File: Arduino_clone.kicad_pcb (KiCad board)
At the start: 2 copper layers, 0 parts

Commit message: Layout design rules edited
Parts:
- added BT1: Battery 3V, Connector_PinHeader_2.54mm:PinHeader_1x02_P2.54mm_Vertical, F.Cu at (151.2, 97.4)
- added C1: 22pF, Capacitor_SMD:C_0805_2012Metric_Pad1.18x1.45mm_HandSolder, F.Cu at (156.0, 96.5)
- added C2: 22pF, Capacitor_SMD:C_0805_2012Metric_Pad1.18x1.45mm_HandSolder, F.Cu at (156.0, 99.6)
- added C3: 10uF, Capacitor_SMD:C_0805_2012Metric_Pad1.18x1.45mm_HandSolder, F.Cu at (150.3, 103.7)
- added D1: LED, LED_SMD:LED_0805_2012Metric_Pad1.15x1.40mm_HandSolder, F.Cu at (150.3, 106.8)
- added J1: Serial, Connector_PinSocket_2.54mm:PinSocket_1x04_P2.54mm_Vertical, F.Cu at (138.4, 64.3)
- added J2: Digital pins, Connector_PinSocket_2.54mm:PinSocket_1x09_P2.54mm_Vertical, F.Cu at (129.2, 64.3)
- added J3: I2C, Connector_PinSocket_2.54mm:PinSocket_1x04_P2.54mm_Vertical, F.Cu at (133.8, 64.3)
- added J4: ICSP, Connector_PinSocket_2.54mm:PinSocket_2x03_P2.54mm_Vertical, F.Cu at (145.6, 64.3)
- added R1: 10k, Resistor_SMD:R_0805_2012Metric_Pad1.20x1.40mm_HandSolder, F.Cu at (155.1, 106.7)
- added R2: 330, Resistor_SMD:R_0805_2012Metric_Pad1.20x1.40mm_HandSolder, F.Cu at (155.1, 103.7)
- added U1: 24LC1025, Package_SO:SOIJ-8_5.3x5.3mm_P1.27mm, F.Cu at (143.6, 93.7)
- added U2: 24LC1025, Package_SO:SOIJ-8_5.3x5.3mm_P1.27mm, F.Cu at (132.2, 105.1)
- added U3: DS1337S+, Package_SO:SO-8_5.3x6.2mm_P1.27mm, F.Cu at (142.7, 105.5)
- added U4: ATMEGA328P-AU, digikey-footprints:TQFP-32_7x7mm, F.Cu at (132.6, 95.9)
- added Y1: 32 MHz, Crystal:Crystal_SMD_MicroCrystal_CC7V-T1A-2Pin_3.2x1.5mm_HandSoldering, F.Cu at (141.7, 98.9)
- added Y2: 16 MHz, Crystal:Crystal_SMD_5032-2Pin_5.0x3.2mm_HandSoldering, F.Cu at (154.0, 92.6)
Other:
- net class Power added: clearance 0.2, trace_width 0.3, via_dia 1, via_drill 0.6

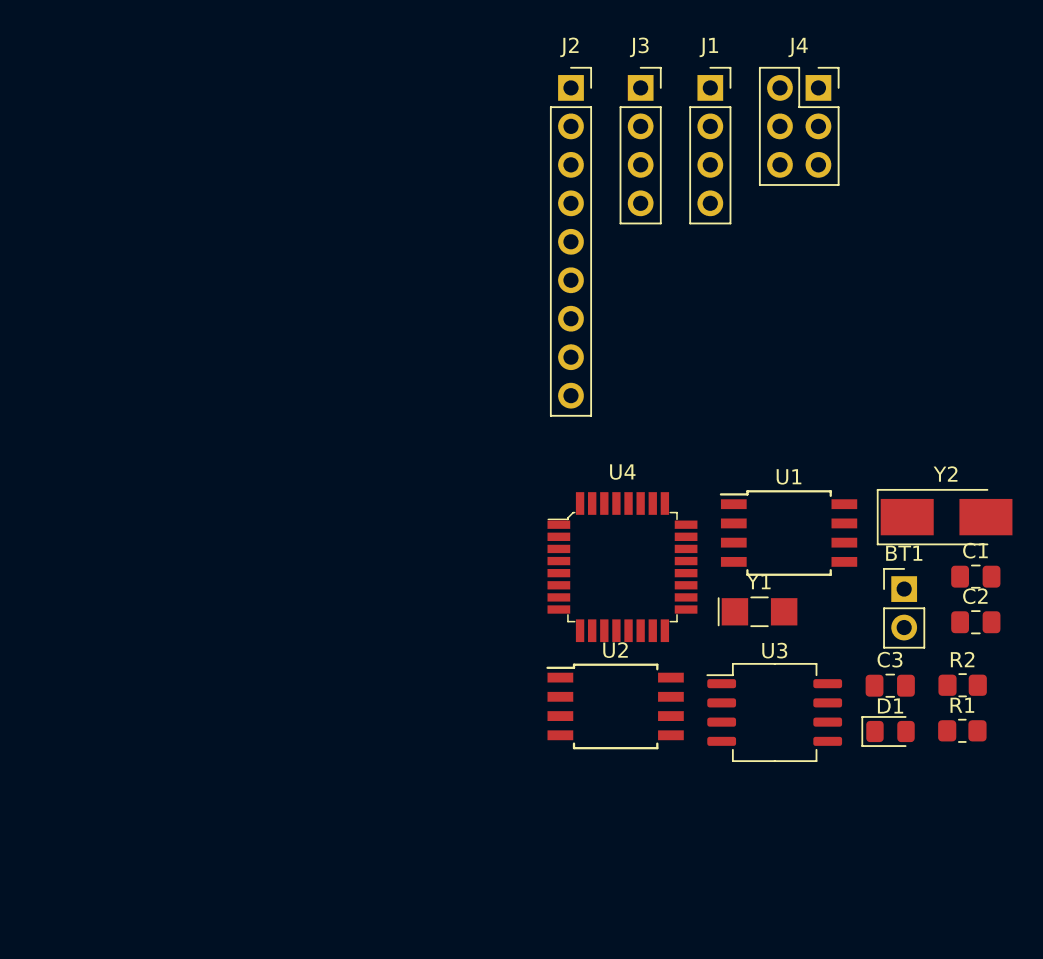
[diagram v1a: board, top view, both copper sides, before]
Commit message: Initial component placement done
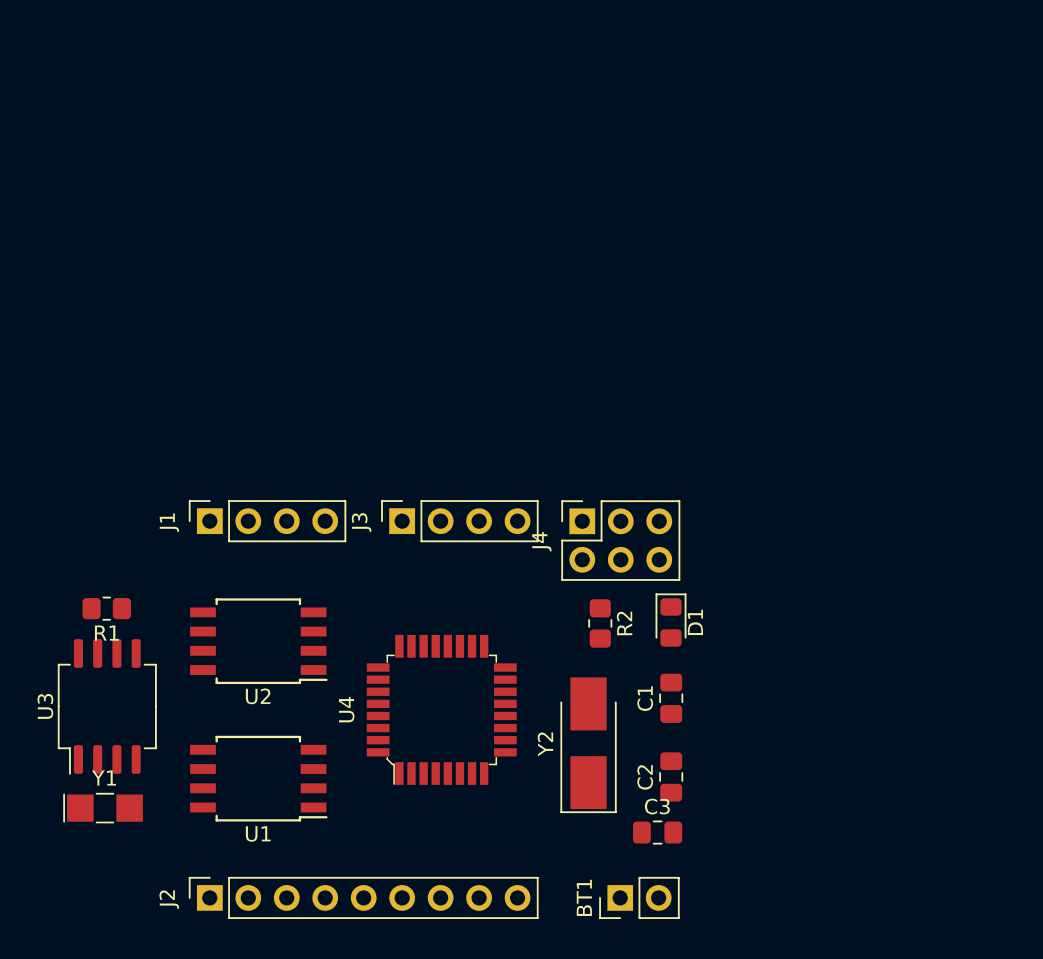
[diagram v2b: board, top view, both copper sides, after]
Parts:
- BT1: value Battery 3V -> 3V
- moved J2 58.6 mm to (105.4, 117.8), turned to 90 degrees
- moved R1 57.1 mm to (98.6, 98.7), turned to 180 degrees
- moved Y1 45.1 mm to (98.5, 111.8)
- moved U3 44.1 mm to (98.6, 105.1), turned to 90 degrees
- moved J1 43.7 mm to (105.4, 92.9), turned to 90 degrees
- moved U1 38.6 mm to (108.6, 109.9), turned to 180 degrees
- moved J3 32.7 mm to (118.1, 92.9), turned to 90 degrees
- moved J4 32.6 mm to (130.0, 92.9), turned to 90 degrees
- moved Y2 28.0 mm to (130.4, 107.5), turned to 90 degrees
- moved BT1 27.7 mm to (132.5, 117.8), turned to 90 degrees
- moved R2 24.3 mm to (131.2, 99.6), turned to 270 degrees
- moved U2 24.0 mm to (108.6, 100.8), turned to 180 degrees
- moved C2 22.6 mm to (135.9, 109.8), turned to 90 degrees
- moved C1 21.7 mm to (135.9, 104.6), turned to 90 degrees
- moved C3 18.2 mm to (135.0, 113.4)
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
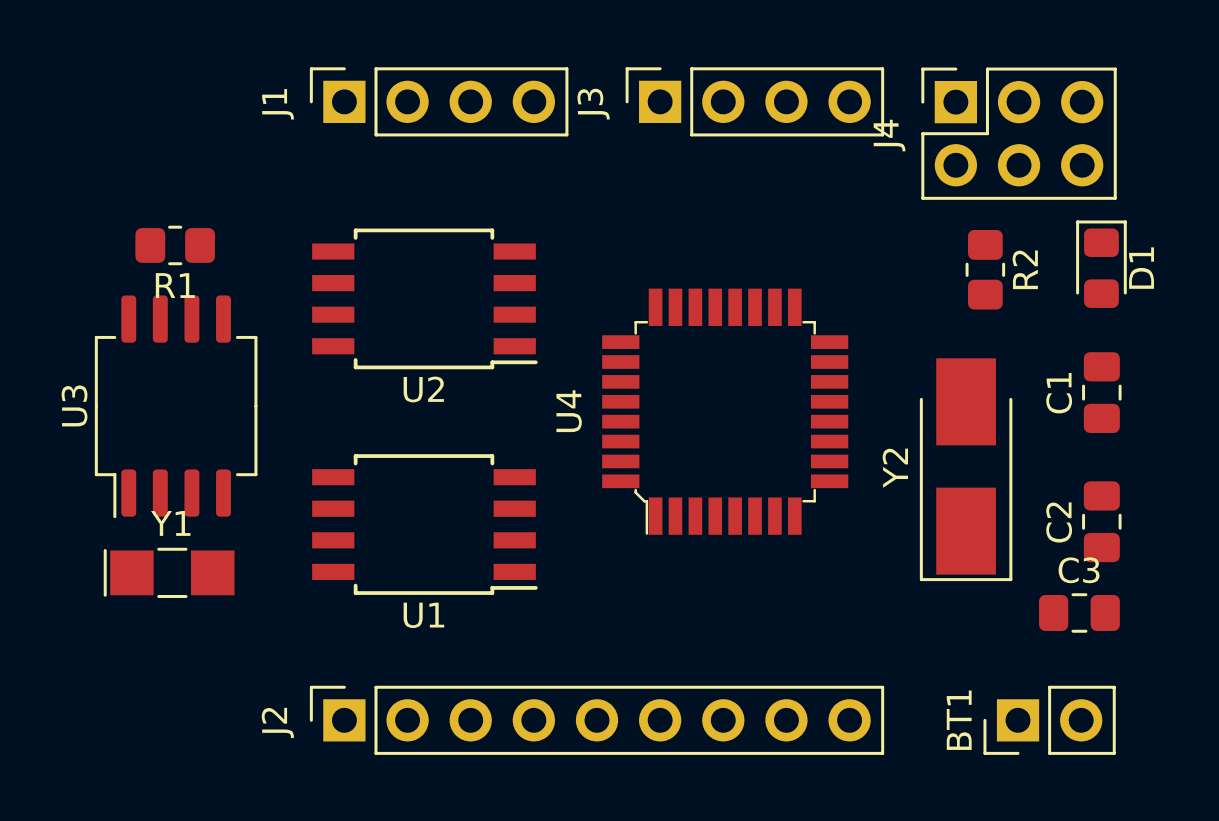
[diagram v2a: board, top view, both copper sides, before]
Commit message: Board outline drawn
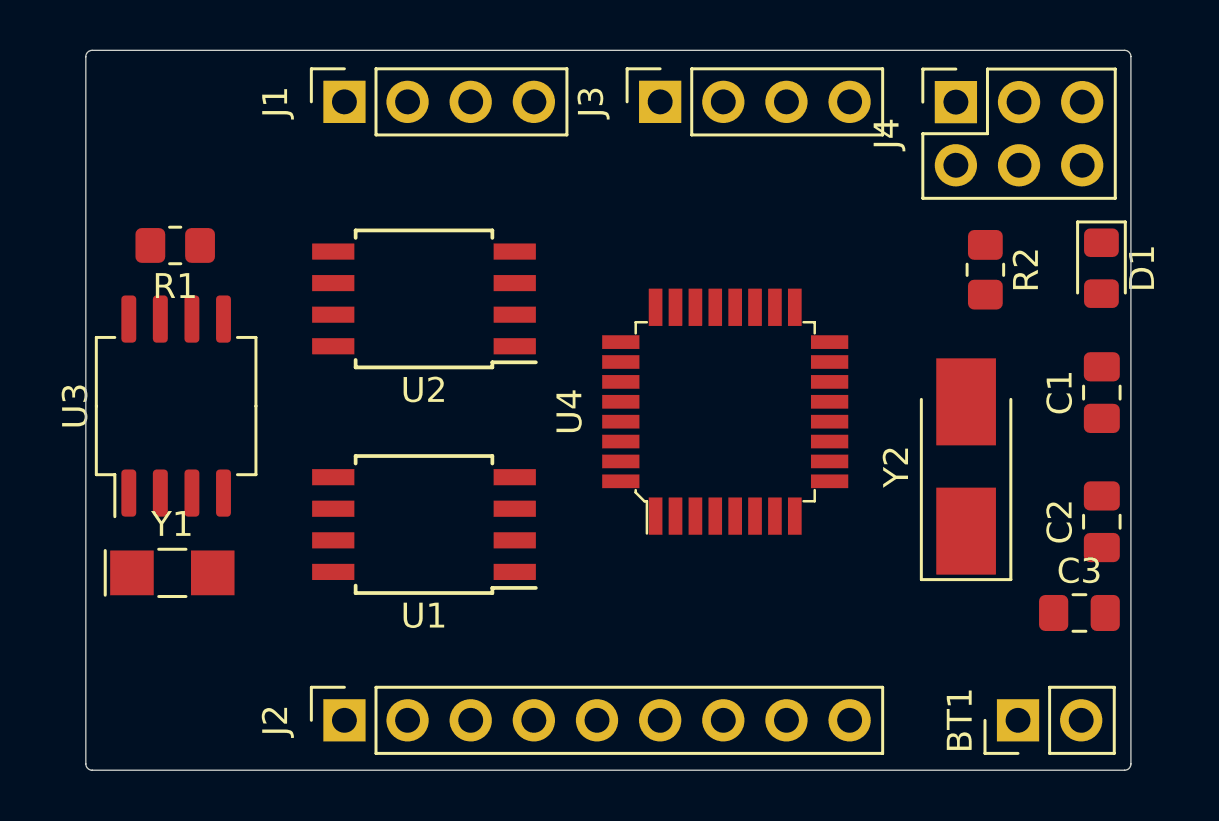
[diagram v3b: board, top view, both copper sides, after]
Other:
- board outline added: 42 x 29 mm
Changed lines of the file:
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@@
   (general
     (thickness 1.6)
-    (drawings 0)
+    (drawings 8)
     (tracks 0)
     (zones 0)
@@
     )
   )
+  (gr_line (start 95.25 90.805) (end 136.779 90.805) (layer Edge.Cuts) (width 0.05))
+  (gr_line (start 94.996 119.507) (end 94.996 91.059) (layer Edge.Cuts) (width 0.05))
+  (gr_line (start 95.25 119.761) (end 136.779 119.761) (layer Edge.Cuts) (width 0.05))
+  (gr_line (start 137.033 91.059) (end 137.033 119.507) (layer Edge.Cuts) (width 0.05))
+  (gr_arc (start 136.779 119.507) (end 136.779 119.761) (angle -90) (layer Edge.Cuts) (width 0.05))
+  (gr_arc (start 95.25 119.507) (end 94.996 119.507) (angle -90) (layer Edge.Cuts) (width 0.05))
+  (gr_arc (start 95.25 91.059) (end 95.25 90.805) (angle -90) (layer Edge.Cuts) (width 0.05))
+  (gr_arc (start 136.779 91.059) (end 137.033 91.059) (angle -90) (layer Edge.Cuts) (width 0.05))
 )

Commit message: Mounting holes added
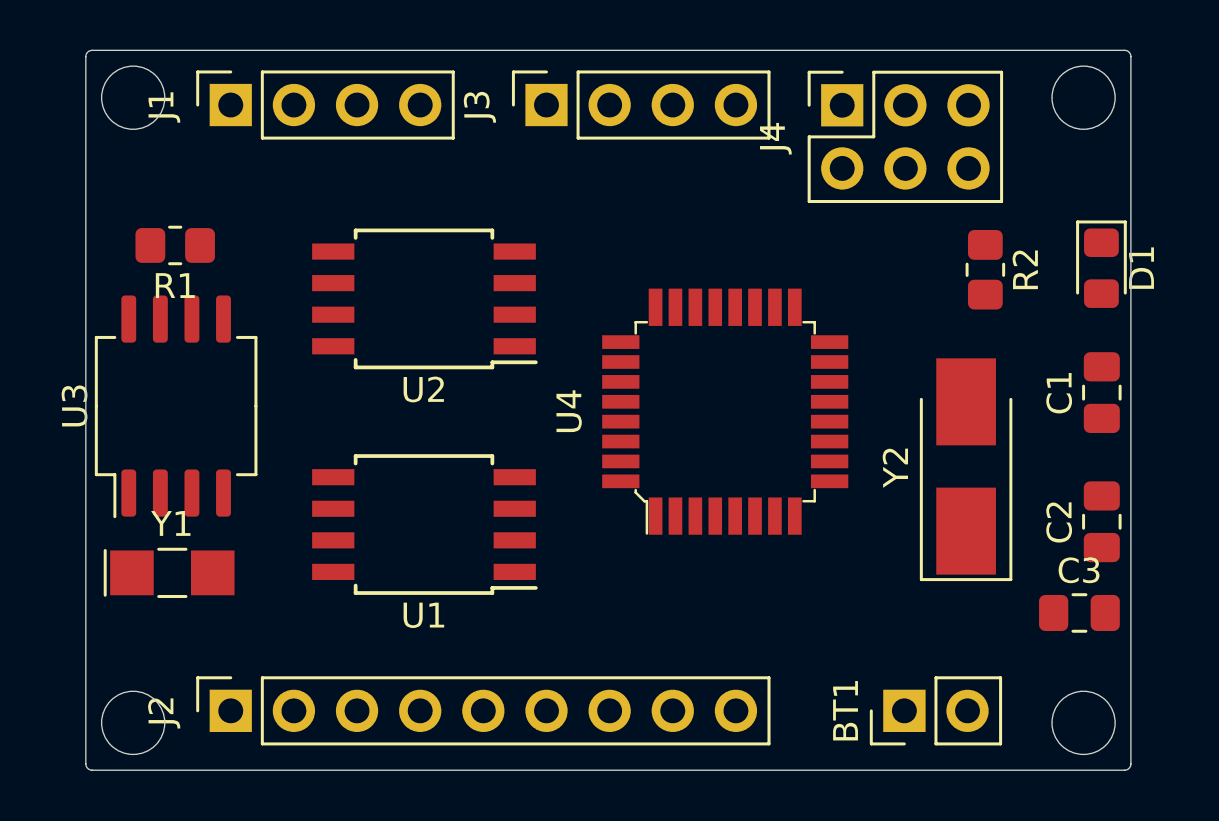
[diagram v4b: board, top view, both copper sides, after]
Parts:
- moved J2 4.59 mm to (100.8, 117.4)
- moved BT1 4.59 mm to (127.9, 117.4)
- moved J1 4.57 mm to (100.8, 93.0)
- moved J3 4.57 mm to (113.5, 93.0)
- moved J4 4.57 mm to (125.4, 93.0)
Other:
- outline, holes or cut-outs redrawn

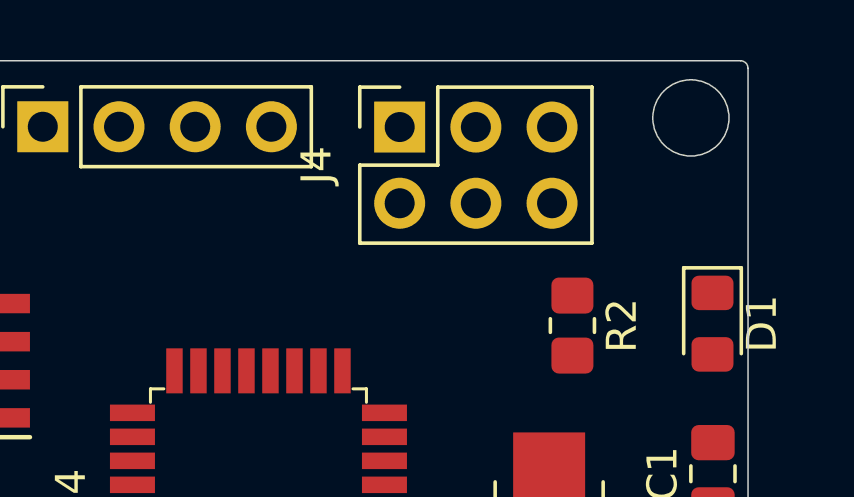
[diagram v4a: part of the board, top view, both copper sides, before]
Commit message: Changed ICSP connector footprint from female to male
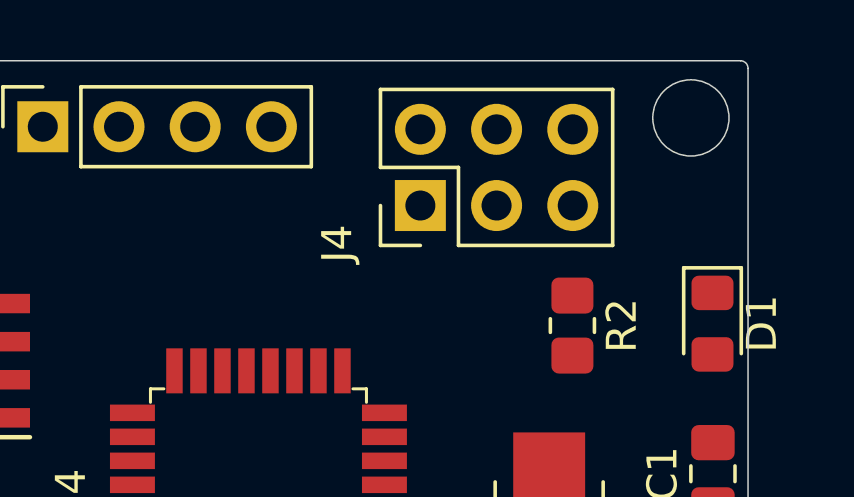
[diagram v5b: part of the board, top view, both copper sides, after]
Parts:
- J4: footprint Connector_PinSocket_2.54mm:PinSocket_2x03_P2.54mm_Vertical -> Connector_PinHeader_2.54mm:PinHeader_2x03_P2.54mm_Vertical
- moved J4 2.71 mm to (126.1, 95.6)
